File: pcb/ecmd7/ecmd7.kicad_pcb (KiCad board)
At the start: 4 copper layers, 120 x 90 mm, 252 parts, among them J1 PMOD_SPI_ENC, J10 SPI Ext., J2 PMOD_ADC_MPIO, J3 PMOD_DRV, J4 Conn_01x02_Socket, J5 Encoder, J6 12V, J7 RS422/BISS-C, J8 5V, J9 FH35C-19S-0.3SHW_99_, Q1 IRFS3806, Q10 BSC098N10NS5, Q11 MMBT3904, Q12 MMBT3904, Q2 IRFS3806, Q3 IRFS3806, Q4 IRFS3806, Q5 IRFS3806, Q6 IRFS3806, Q7 BSC098N10NS5, Q8 BSC098N10NS5, Q9 BSC098N10NS5, U1 TMC6200-TA, U10 FIN1002M5X, U11 FIN1002M5X, U12 FIN1002M5X, U13 ADM3490ExR, U14 LM5118MH, U15 74LVC1G139, U16 MB85RS1MT, U2 MCP33151-05T-E/MN, U3 LM5118MH, U4 MCP33151-05T-E/MN, U5 MCP33151-05T-E/MN, U6 TLV71318PDBV, U7 MCP33151-05T-E/MN, U8 TLV803EA30DBZ, U9 LT1616ES6#TRPBF

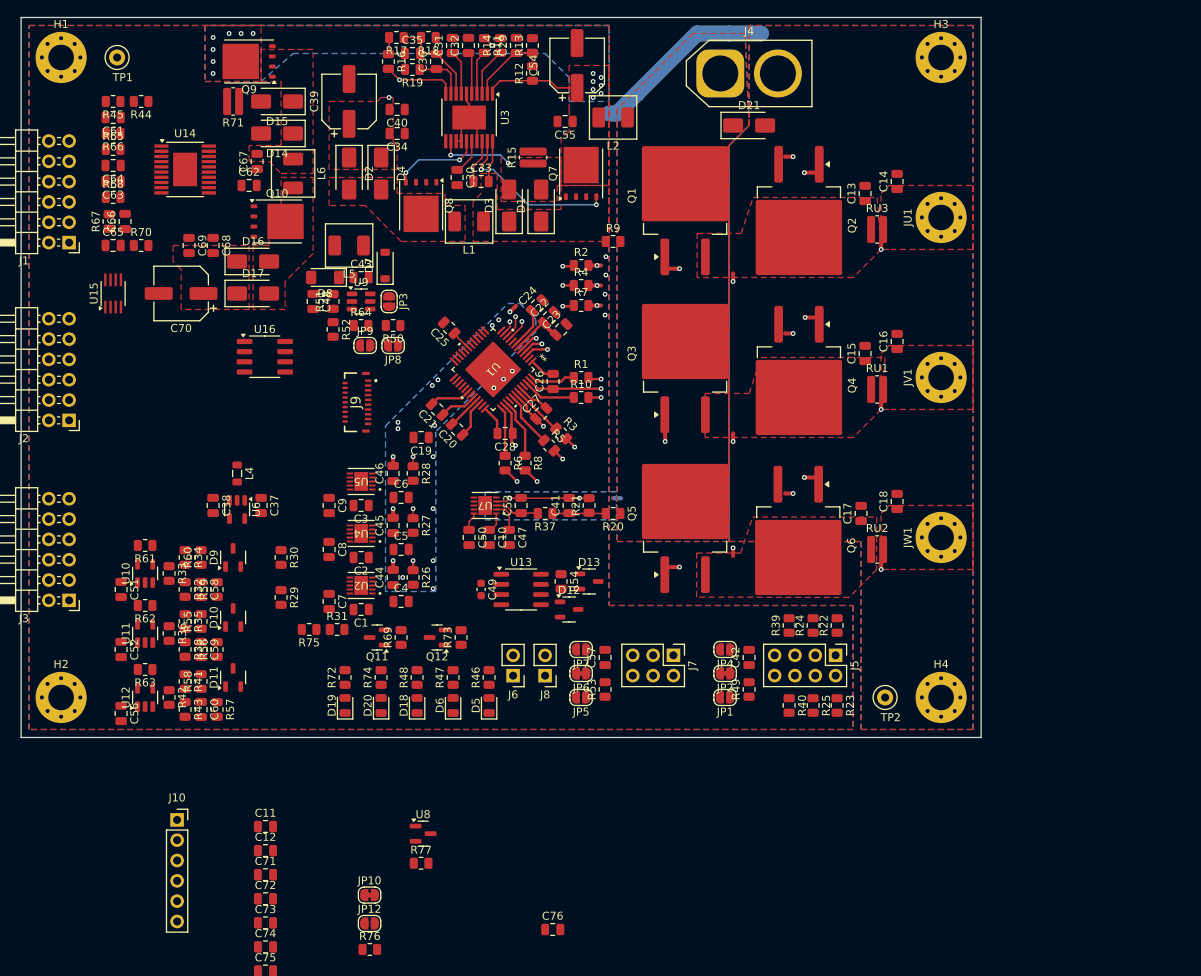
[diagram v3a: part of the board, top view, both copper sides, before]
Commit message: WIP: Partial routing
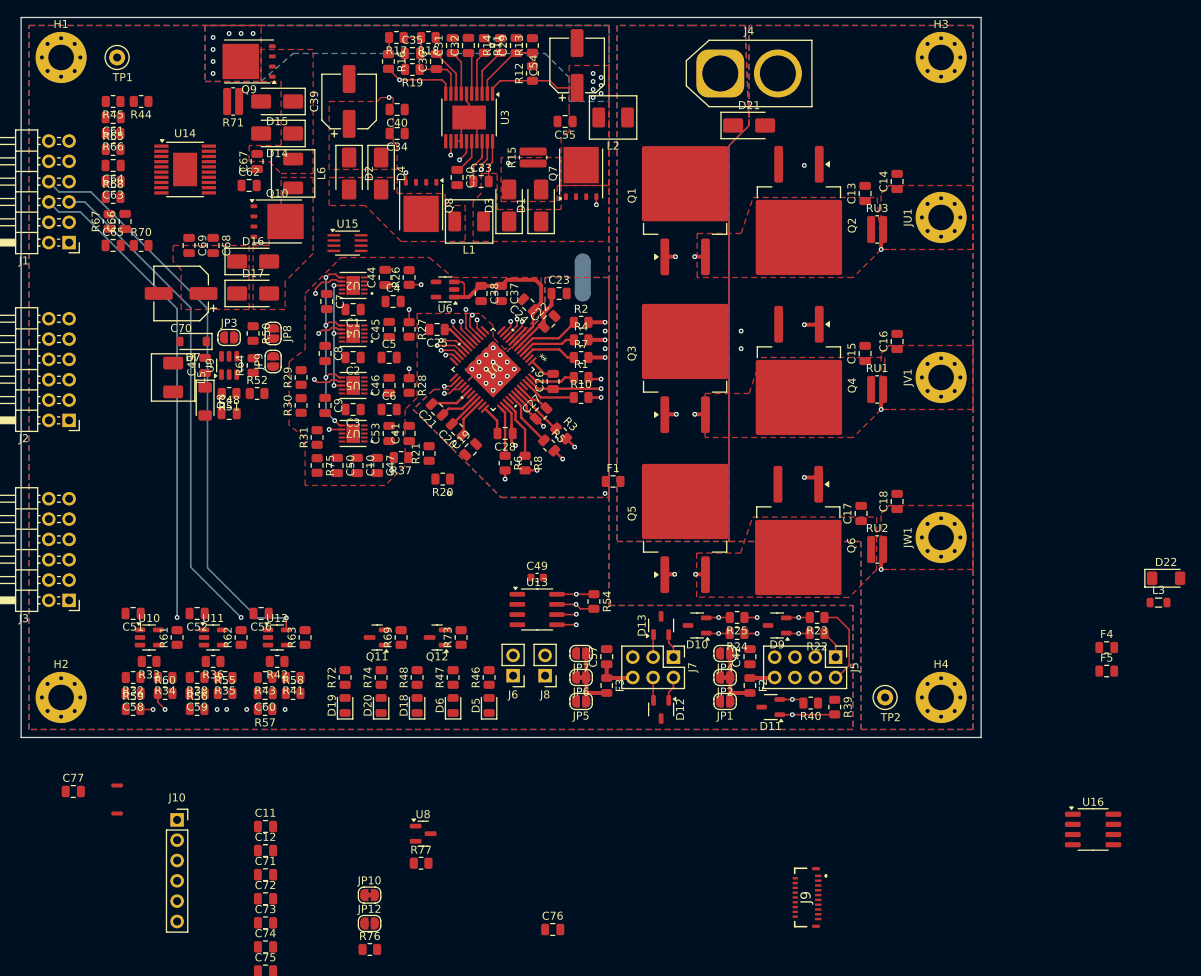
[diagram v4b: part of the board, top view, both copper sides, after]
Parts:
- removed L4: 1u, Inductor_SMD:L_0805_2012Metric
- removed NTGU1, NTGV1, NTGW1, NTPV2, NTPW3: NetTie_2, NetTie:NetTie-2_SMD_Pad0.5mm
- removed R49, R53: 10, Resistor_SMD:R_0805_2012Metric
- removed R9: 0.47, Resistor_SMD:R_0805_2012Metric
- added C77: 100n, Capacitor_SMD:C_0805_2012Metric, F.Cu at (66.5, 136.8)
- added D22: BZV55B3V6, Diode_SMD:D_MiniMELF, F.Cu at (203.1, 110.1)
- added F1: Polyfuse, Fuse:Fuse_0805_2012Metric, F.Cu at (134.0, 98.0)
- added F2: Polyfuse, Fuse:Fuse_0805_2012Metric, F.Cu at (151.1, 123.5)
- added F3: Polyfuse, Fuse:Fuse_0805_2012Metric, F.Cu at (133.2, 123.5)
- added F4: Polyfuse, Fuse:Fuse_0805_2012Metric, F.Cu at (195.7, 118.8)
- added F5: Polyfuse, Fuse:Fuse_0805_2012Metric, F.Cu at (195.7, 121.7)
- added L3: 10uH, Inductor_SMD:L_0805_2012Metric, F.Cu at (202.2, 113.1)
- added NTP2G2: NetTie_2, NetTie:NetTie-2_SMD_Pad0.5mm, F.Cu at (72.0, 136.0)
- added NTP2G3: NetTie_2, NetTie:NetTie-2_SMD_Pad0.5mm, F.Cu at (72.0, 139.5)
- moved U16 119.2 mm to (194.0, 141.5)
- moved J9 83.6 mm to (158.1, 150.0)
- moved D9 68.5 mm to (154.5, 116.0), turned to 180 degrees
- moved D11 67.3 mm to (153.7, 126.2), turned to 180 degrees
- moved D10 58.0 mm to (144.5, 116.0), turned to 180 degrees
- moved C38 42.7 mm to (117.5, 74.5)
- moved C37 40.0 mm to (120.0, 74.5)
- moved U6 37.8 mm to (113.0, 74.0), turned to 180 degrees
- moved C1 37.5 mm to (101.5, 76.5)
- moved C4 37.5 mm to (106.5, 75.5)
- moved C44 37.5 mm to (105.5, 72.5)
- moved U2 37.5 mm to (101.5, 73.5)
- moved R26 37.5 mm to (108.5, 72.5), turned to 90 degrees
- moved C7 37.5 mm to (98.2, 75.5)
- moved NTP2G1 36.6 mm to (130.2, 72.5), turned to 90 degrees
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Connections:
- net VMOT_REF renamed Net-(U7-AIN-)
- C1 pad 2: GND -> GNDA
- C10 pad 2: GND -> GNDA
- C19 pad 2: GND -> GNDPWR
- C2 pad 2: GND -> GNDA
- C22 pad 2: GND -> GNDPWR
- C23 pad 2: GND -> GNDPWR
- C24 pad 2: GND -> GNDA
- C3 pad 2: GND -> GNDA
- C37 pad 1: Net-(U6-EN) -> +5VA
- C37 pad 2: GND -> GNDA
- C38 pad 1: Net-(U6-EN) -> +5VA
- C38 pad 2: GND -> GNDA
- C4 pad 2: GND -> GNDA
- C44 pad 2: I_REF -> GNDA
- C45 pad 2: I_REF -> GNDA
- C46 pad 2: I_REF -> GNDA
- C47 pad 2: GND -> GNDA
- C5 pad 2: GND -> GNDA
- C50 pad 1: +3.3V -> +3.3VA
- C50 pad 2: GND -> GNDA
- C6 pad 2: GND -> GNDA
- C7 pad 1: +3.3V -> +3.3VA
- C7 pad 2: GND -> GNDA
- C71 pad 1: +3.3V -> /3V3_DISP
- C8 pad 1: +3.3V -> +3.3VA
- C8 pad 2: GND -> GNDA
- C9 pad 1: +3.3V -> +3.3VA
- C9 pad 2: GND -> GNDA
- D10 pad 1: /ADC+IO/B_LS_N -> /ADC+IO/A_LS_N
- D10 pad 2: /ADC+IO/B_LS_P -> /ADC+IO/A_LS_P
- D12 pad 1: RS422_TX_B -> RS422_TX_A
- D12 pad 2: RS422_TX_A -> RS422_TX_B
- D13 pad 1: RS422_RX_A -> RS422_RX_B
- D13 pad 2: RS422_RX_B -> RS422_RX_A
- D9 pad 1: /ADC+IO/A_LS_N -> /ADC+IO/B_LS_N
- D9 pad 2: /ADC+IO/A_LS_P -> /ADC+IO/B_LS_P
- J1 pad 5: ENC_A -> ENC_B
- J1 pad 6: ENC_B -> ENC_A
- J10 pad 1: +3.3V -> Net-(J10-Pin_1)
- J3 pad 10: /UH -> /VH
- J3 pad 11: /DRV_EN -> /UL
- J3 pad 12: /FAULT -> /UH
- J3 pad 5: /WL -> /DRV_EN
- J3 pad 6: /WH -> /FAULT
- J3 pad 7: /VL -> /WL
- J3 pad 8: /VH -> /WH
- J3 pad 9: /UL -> /VL
- J5 pad 1: ENC_A_N -> ENC_B_N
- J5 pad 2: ENC_A_P -> ENC_B_P
- J5 pad 3: ENC_B_N -> ENC_A_P
- J5 pad 4: ENC_B_P -> ENC_Z_N
- J5 pad 5: ENC_Z_N -> ENC_A_N
- J7 pad 1: RS422_TX_B -> RS422_RX_A
- J7 pad 4: RS422_RX_A -> RS422_TX_B
- J9 pad 11: +3.3V -> /3V3_DISP
- J9 pad 12: +3.3V -> /3V3_DISP
- J9 pad 14: +3.3V -> /3V3_DISP
- R20 pad 1: VMot -> Vdrive
- R22 pad 1: ENC_A_N -> ENC_B_N
- R22 pad 2: /ADC+IO/A_LS_N -> /ADC+IO/B_LS_N
- R23 pad 1: ENC_A_P -> ENC_B_P
- R23 pad 2: /ADC+IO/A_LS_P -> /ADC+IO/B_LS_P
- R24 pad 1: ENC_B_N -> ENC_A_N
- R24 pad 2: /ADC+IO/B_LS_N -> /ADC+IO/A_LS_N
- R25 pad 1: ENC_B_P -> ENC_A_P
- R25 pad 2: /ADC+IO/B_LS_P -> /ADC+IO/A_LS_P
- R29 pad 2: +3.3V -> +3.3VA
- R30 pad 1: GND -> GNDA
- R31 pad 2: +3.3V -> +3.3VA
- R75 pad 2: GND -> GNDA
- U1 pad 8: GND -> GNDA
- U1 pad EPAD: GND -> GNDPWR
- U2 pad 10: +3.3V -> +3.3VA
- U2 pad 4: I_REF -> GNDA
- U2 pad 5: GND -> GNDA
- U4 pad 10: +3.3V -> +3.3VA
- U4 pad 4: I_REF -> GNDA
- U4 pad 5: GND -> GNDA
- U5 pad 10: +3.3V -> +3.3VA
- U5 pad 4: I_REF -> GNDA
- U5 pad 5: GND -> GNDA
- U6 pad 1: Net-(U6-EN) -> +5VA
- U6 pad 2: GND -> GNDA
- U6 pad 3: Net-(U6-EN) -> +5VA
- U7 pad 5: GND -> GNDA
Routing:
- net GND: track 119.7 -> 10.5 mm, vias 10 -> 0
- net /ADC+IO/A_LS_P: track 0.00 -> 82.4 mm, vias 0 -> 2
- net /ADC+IO/B_LS_P: track 0.00 -> 81.4 mm, vias 0 -> 2
- net /ADC+IO/A_LS_N: track 0.00 -> 81.1 mm, vias 0 -> 2
- net /ADC+IO/B_LS_N: track 0.00 -> 79.4 mm, vias 0 -> 2
- net ENC_Z: track 0.00 -> 72.8 mm, vias 0 -> 1
- net /ADC+IO/Z_LS_P: track 0.00 -> 72.8 mm, vias 0 -> 2
- net /ADC+IO/Z_LS_N: track 0.00 -> 70.6 mm, vias 0 -> 2
- net /SPI_SDO: track 0.00 -> 65.1 mm, vias 0 -> 1
- net /UH: track 0.00 -> 64.6 mm, vias 0 -> 1
- net /SPI_SDI: track 0.00 -> 63.2 mm, vias 0 -> 1
- net ENC_B: track 0.00 -> 62.0 mm, vias 0 -> 1
- net /WH: track 0.00 -> 61.9 mm, vias 0 -> 1
- net /VH: track 0.00 -> 61.8 mm, vias 0 -> 1
- net /SPI_SCK: track 0.00 -> 61.1 mm, vias 0 -> 1
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- added copper zone on F.Cu, net GNDA
- added copper zone on In1.Cu, net GNDA
- added copper zone on In1.Cu, net GNDPWR
- added copper zone on In2.Cu, net GNDPWR
- removed copper zone on B.Cu, net I_REF
- removed copper zone on In1.Cu, net I_REF
- removed copper zone on In2.Cu, net I_REF
- removed copper zone on B.Cu, net Net-(U7-AIN-)

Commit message: WIP: advnced  routing
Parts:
- added TP3: U, TestPoint:TestPoint_Loop_D2.50mm_Drill1.0mm, F.Cu at (170.5, 68.7)
- added TP4: V, TestPoint:TestPoint_Loop_D2.50mm_Drill1.0mm, F.Cu at (170.5, 88.8)
- added TP5: W, TestPoint:TestPoint_Loop_D2.50mm_Drill1.0mm, F.Cu at (170.4, 108.7)
- moved NTP2G2 77.4 mm to (116.0, 72.3), turned to -90 degrees
- moved C65 6.00 mm to (71.5, 62.5)
- moved R68 6.00 mm to (71.5, 68.5)
- moved R71 1.51 mm to (86.3, 52.0)
- moved C7 0.61 mm to (98.3, 76.1)
- moved C66 0.50 mm to (72.5, 65.5)
- moved R67 0.50 mm to (70.5, 65.5)
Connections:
- J10 pad 6: /CS_FRAM -> /CS_EXT
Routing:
- net +12V: track 21.0 -> 88.0 mm, vias 2 -> 12
- net +5VA: track 23.8 -> 69.8 mm, vias 0 -> 5
- net Net-(U2-SDI): track 0.00 -> 37.2 mm, vias 0 -> 4
- net +3.3VA: track 0.00 -> 34.3 mm, vias 0 -> 4
- net VSupply: track 13.4 -> 36.0 mm, vias 15 -> 17
- net Net-(Q9-G): track 0.00 -> 22.4 mm, vias 0 -> 2
- net Net-(Q10-G): track 0.00 -> 12.2 mm, vias 0 -> 2
- net Net-(U14-COMP): track 0.00 -> 10.9 mm
- net Net-(D14-A): track 0.00 -> 9.03 mm, vias 0 -> 2
- net Net-(U14-FB): track 0.00 -> 8.02 mm
- net Net-(U14-UVLO): track 0.00 -> 6.97 mm
- net Net-(U14-HB): track 0.00 -> 6.68 mm
- net AD_SCK: track 53.9 -> 60.4 mm
- net Net-(U14-RT): track 0.00 -> 6.49 mm
- net Net-(D14-K): track 0.00 -> 6.43 mm
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- added copper zone on B.Cu, net +12V
- added copper zone on In1.Cu, net +12V
- added copper zone on In2.Cu, net +12V
- added copper zone on F.Cu, net Net-(D14-A)

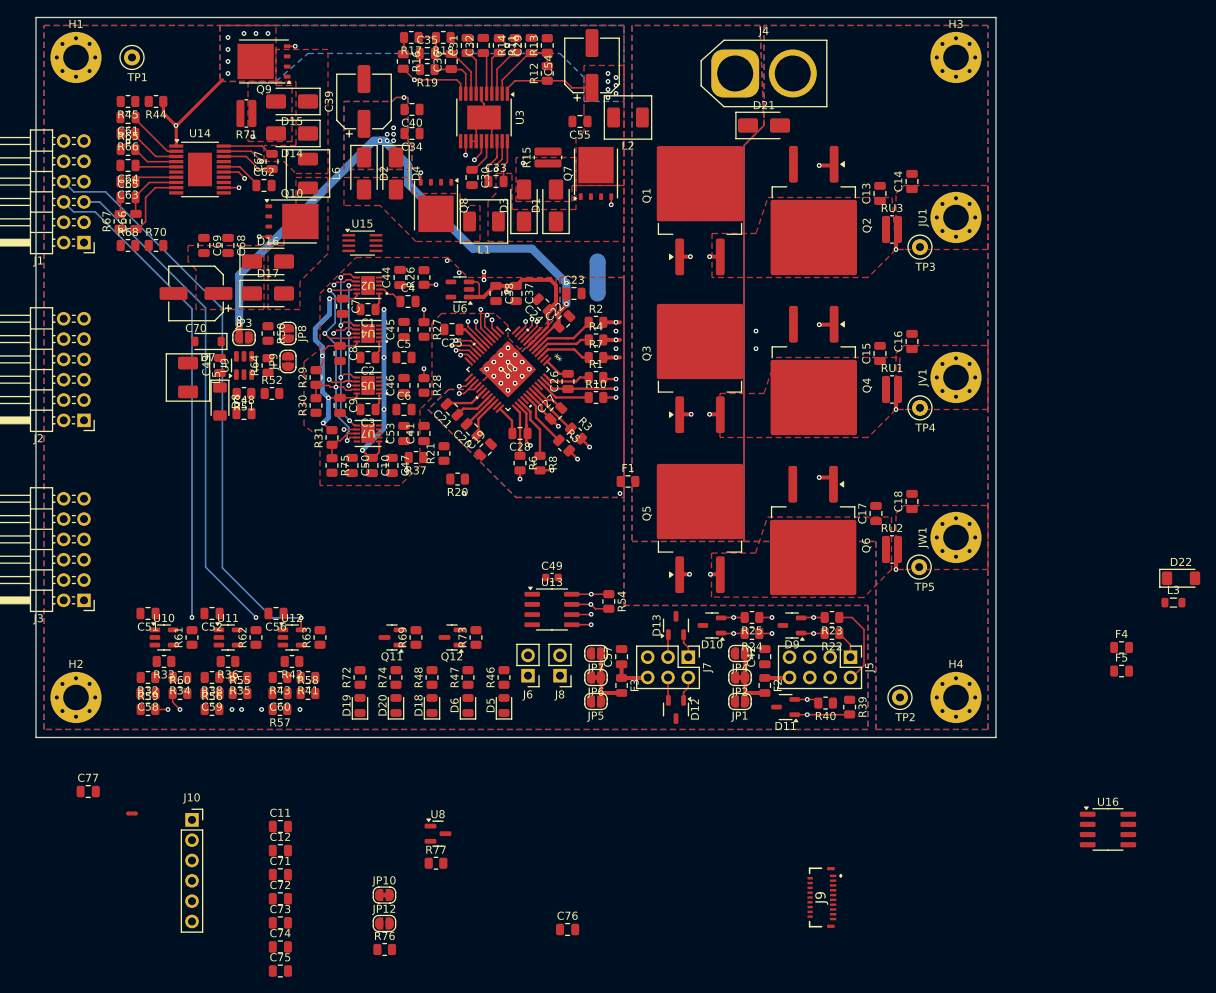
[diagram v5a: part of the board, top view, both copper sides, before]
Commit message: Routing complete, DRC successful
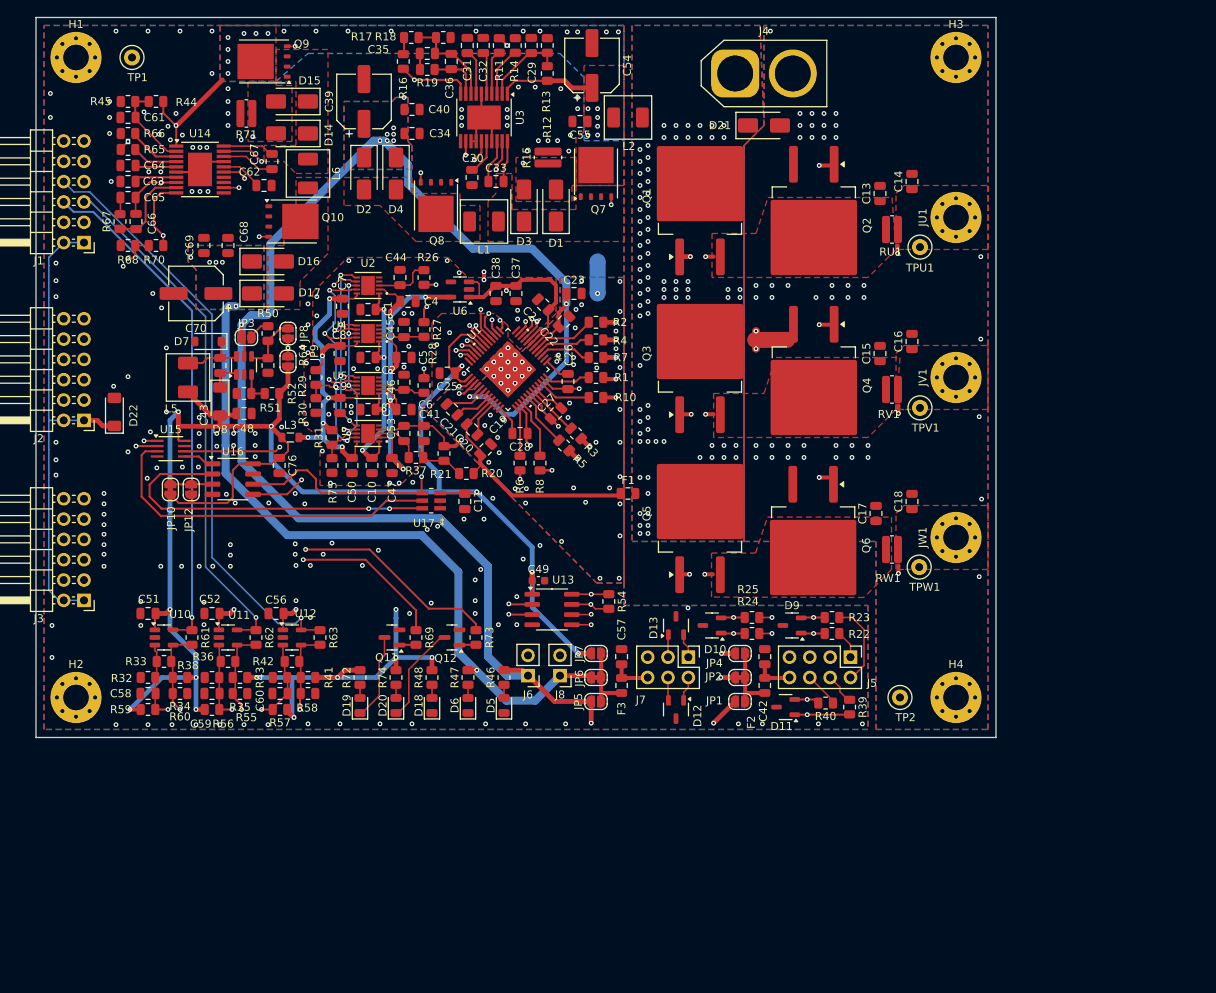
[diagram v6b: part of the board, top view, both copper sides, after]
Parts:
- removed C12: 1u, Capacitor_SMD:C_0805_2012Metric
- removed C71, C74, C75, C77: 100n, Capacitor_SMD:C_0805_2012Metric
- removed C72, C73: 10u, Capacitor_SMD:C_0805_2012Metric
- removed F4, F5: Polyfuse, Fuse:Fuse_0805_2012Metric
- removed J10: SPI Ext., Connector_PinSocket_2.54mm:PinSocket_1x06_P2.54mm_Vertical
- removed J9: FH35C-19S-0.3SHW_99_, SSTA:FH35C19S03SHW99
- removed R76, R77: 10k, Resistor_SMD:R_0805_2012Metric
- removed U8: TLV803EA30DBZ, Package_TO_SOT_SMD:SOT-23
- added NTP2G4: NetTie_2, NetTie:NetTie-2_SMD_Pad2.0mm, F.Cu at (151.9, 80.3)
- added U17: TMP122AIDBVR, SSTA:DBV6, F.Cu at (109.4, 100.4)
- C11: value 1u -> 100n
- moved D22 134.9 mm to (69.8, 89.3), turned to 90 degrees
- moved U16 117.8 mm to (84.6, 97.7)
- moved L3 112.3 mm to (91.8, 92.5)
- moved C76 68.3 mm to (90.4, 96.0), turned to -90 degrees
- moved NTP2G3 61.7 mm to (112.8, 93.2), turned to 45 degrees
- moved JP12 59.4 mm to (79.4, 99.0), turned to 90 degrees
- moved JP10 57.3 mm to (76.8, 99.0), turned to -90 degrees
- moved C11 46.7 mm to (113.6, 100.5), turned to -90 degrees
- moved U15 35.1 mm to (76.8, 93.9)
- moved C25 5.48 mm to (111.4, 84.5)
- moved C49 1.75 mm to (122.8, 110.4)
- moved F1 1.50 mm to (134.0, 99.5)
- moved R20 1.30 mm to (113.8, 97.0)
- moved NTPW1 0.70 mm to (144.1, 109.6)
- moved NTSV1 0.58 mm to (167.8, 89.0)
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- renumbered RU3 to RU1, RU1 to RV1, RU2 to RW1, TP3 to TPU1, TP4 to TPV1, TP5 to TPW1
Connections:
- net /CS_0 renamed CS0
- net /CS_1 renamed CS1
- net /CS_DRV renamed ~{CS_DRV}
- net /SPI_SCK renamed SPI_SCK
- net /SPI_SDI renamed SPI_SDI
- net /SPI_SDO renamed SPI_SDO
- net CS_AD renamed ~{CS_AD}
- net Vdrive renamed VDrv
- C11 pad 1: Net-(C11-Pad1) -> +3.3V
- C11 pad 2: Net-(C11-Pad2) -> GND
- C13 pad 2: GNDPWR -> GNDMOT
- C14 pad 2: GNDPWR -> GNDMOT
- C15 pad 2: GNDPWR -> GNDMOT
- C16 pad 2: GNDPWR -> GNDMOT
- C17 pad 2: GNDPWR -> GNDMOT
- C18 pad 2: GNDPWR -> GNDMOT
- C19 pad 2: GNDPWR -> GNDDRV
- C22 pad 2: GNDPWR -> GNDDRV
- C23 pad 2: GNDPWR -> GNDDRV
- D21 pad 2: GNDPWR -> GNDMOT
- H3 pad 1: GNDPWR -> GNDMOT
- H4 pad 1: GNDPWR -> GNDMOT
- J4 pad 2: GNDPWR -> GNDMOT
- NTP2G1 pad 1: GNDPWR -> GNDDRV
- NTP2G3 pad 2: GNDPWR -> GNDDRV
- Q2 pad 3: GNDPWR -> GNDMOT
- Q4 pad 3: GNDPWR -> GNDMOT
- Q6 pad 3: GNDPWR -> GNDMOT
- TP2 pad 1: GNDPWR -> GNDMOT
- U1 pad EPAD: GNDPWR -> GNDDRV
- U15 pad 3: /CS_FRAM -> /ADC+IO/~{CS_TMP}
- U15 pad 5: /CS_DISP -> /ADC+IO/~{CS_FRAM}
- U15 pad 7: /CS_EXT -> unconnected-(U15-Y0-Pad7)
- U16 pad 1: /CS_FRAM -> /ADC+IO/~{CS_FRAM}
- U7 pad 10: +3.3V -> +3.3VA
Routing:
- net +3.3V: track 3.89 -> 318.6 mm, vias 0 -> 19
- net +12V: track 88.0 -> 220.2 mm, vias 12 -> 13
- net +5V: track 0.00 -> 125.0 mm, vias 0 -> 9
- net +3.3V_IO: track 0.00 -> 91.0 mm, vias 0 -> 1
- net SPI_SDO: track 65.1 -> 147.3 mm, vias 1 -> 3
- net RS422_TX: track 0.00 -> 75.6 mm, vias 0 -> 1
- net RS422_RX: track 0.00 -> 73.6 mm, vias 0 -> 1
- net ~{CS_DRV}: track 0.00 -> 63.7 mm, vias 0 -> 2
- net SPI_SDI: track 63.2 -> 117.2 mm, vias 1 -> 2
- net SPI_SCK: track 61.1 -> 114.6 mm, vias 1 -> 2
- net +1V8A: track 3.27 -> 51.2 mm, vias 0 -> 5
- net /ADC+IO/~{CS_TMP}: track 0.00 -> 44.2 mm
- net CS0: track 0.00 -> 41.9 mm, vias 0 -> 1
- net CS1: track 0.00 -> 38.4 mm, vias 0 -> 1
- net GNDDRV: track 0.00 -> 36.2 mm, vias 0 -> 57
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- added copper zone on B.Cu, net +5V
- added copper zone on In1.Cu, net +5V
- added copper zone on In2.Cu, net +5V
- added copper zone on B.Cu, net GNDDRV
- added copper zone on F.Cu, net GNDDRV
- added copper zone on In1.Cu, net GNDDRV
- added copper zone on In2.Cu, net GNDDRV
- added copper zone on B.Cu, net GNDMOT
- added copper zone on F.Cu, net GNDMOT
- added copper zone on In1.Cu, net GNDMOT
- added copper zone on In2.Cu, net GNDMOT
- removed copper zone on B.Cu, net GNDPWR
- removed copper zone on F.Cu, net GNDPWR
- removed copper zone on In1.Cu, net GNDPWR
- removed copper zone on In2.Cu, net GNDPWR
